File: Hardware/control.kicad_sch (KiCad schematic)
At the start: 4 parts, among them U1 RP2354B, U2 SN74LVC245APW, U3 SN74LVC245APW, U4 SN74LVC8T245

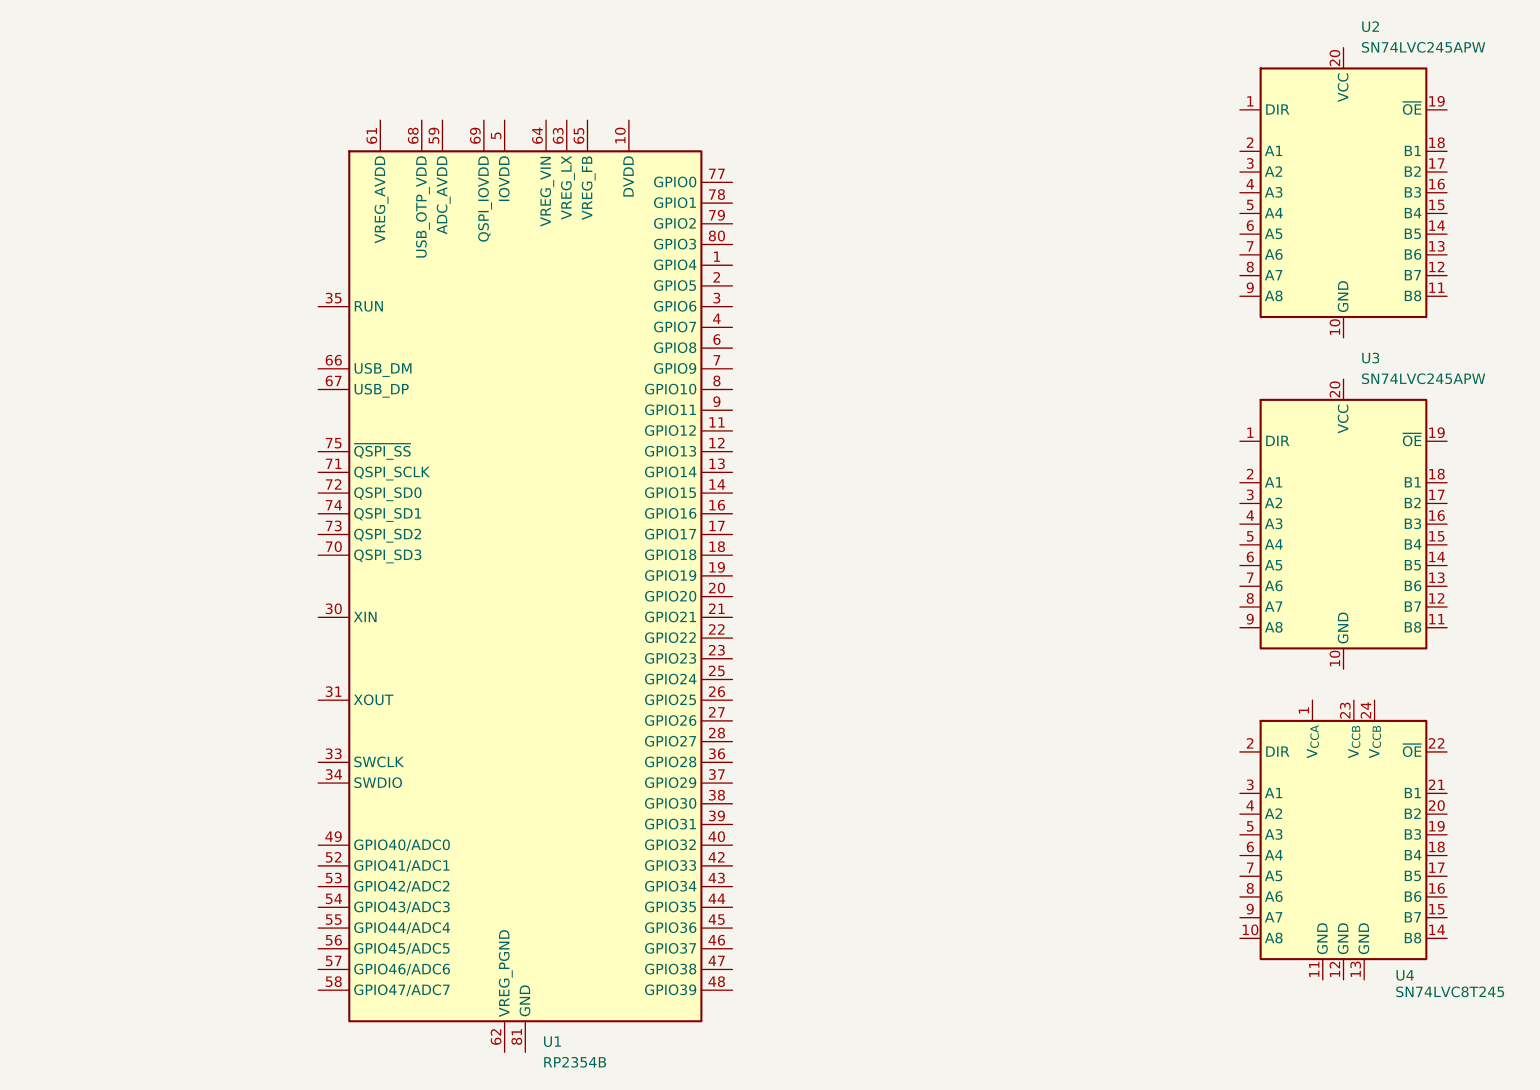
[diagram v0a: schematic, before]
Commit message: fix kicad project hierarchy
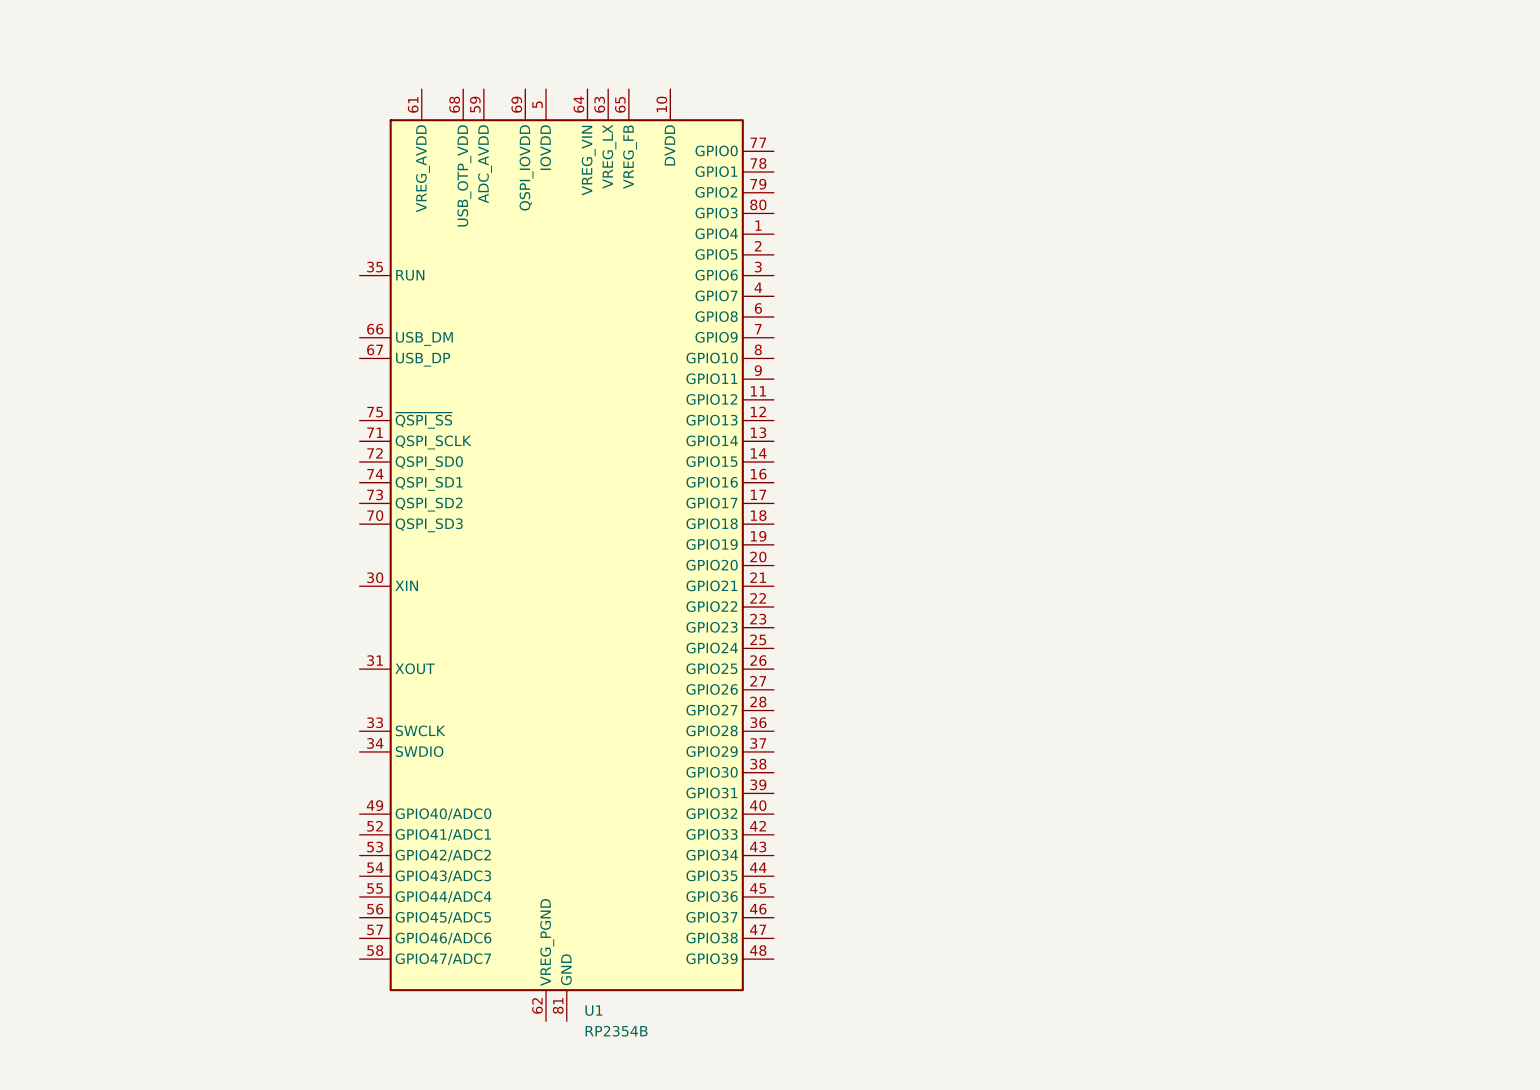
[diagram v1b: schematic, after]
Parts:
- removed U2, U3: SN74LVC245APW, Package_SO:TSSOP-20_4.4x6.5mm_P0.65mm, symbol Logic_LevelTranslator:SN74LVC245APW
- removed U4: SN74LVC8T245, symbol Logic_LevelTranslator:SN74LVC8T245

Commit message: finish digitalker
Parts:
- added X2: ABM8-272-T3, symbol Digichiver:ABM8-272-T3
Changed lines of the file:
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@@
+	)
+	(symbol
+		(lib_id "Digichiver:ABM8-272-T3")
+		(at 165.1 130.81 0)
+		(unit 1)
+		(body_style 1)
+		(exclude_from_sim no)
+		(in_bom yes)
+		(on_board yes)
+		(in_pos_files yes)
+		(dnp no)
+		(fields_autoplaced yes)
+		(property "Reference" "X2"
+			(at 165.1 127 0)
+			(show_name no)
+			(do_not_autoplace no)
+			(effects
+				(font
+					(size 1.27 1.27)
+				)
+			)
+		)
+		(property "Value" "ABM8-272-T3"
+			(at 165.1 129.54 0)
+			(show_name no)
+			(do_not_autoplace no)
+			(effects
+				(font
+					(size 1.27 1.27)
+				)
+			)
+		)
+		(property "Footprint" ""
+			(at 165.1 130.81 0)
+			(hide yes)
+			(show_name no)
+			(do_not_autoplace no)
+			(effects
+				(font
+					(size 1.27 1.27)
+				)
+			)
+		)
+		(property "Datasheet" ""
+			(at 165.1 130.81 0)
+			(hide yes)
+			(show_name no)
+			(do_not_autoplace no)
+			(effects
+				(font
+					(size 1.27 1.27)
+				)
+			)
+		)
+		(property "Description" ""
+			(at 165.1 130.81 0)
+			(hide yes)
+			(show_name no)
+			(do_not_autoplace no)
+			(effects
+				(font
+					(size 1.27 1.27)
+				)
+			)
+		)
+		(pin "1"
+		)
+		(pin "2"
+		)
+		(pin "3"
+		)
+		(pin "4"
+		)
+		(instances
+			(project "digichiver"
+				(path "/51de4045-d2a2-42d9-b145-319acd726bb6/7bd3bb5c-26f1-47ae-a373-5b3a637c22c5"
+					(reference "X2")
+					(unit 1)
+				)
+			)
+		)
 	)
 	(symbol

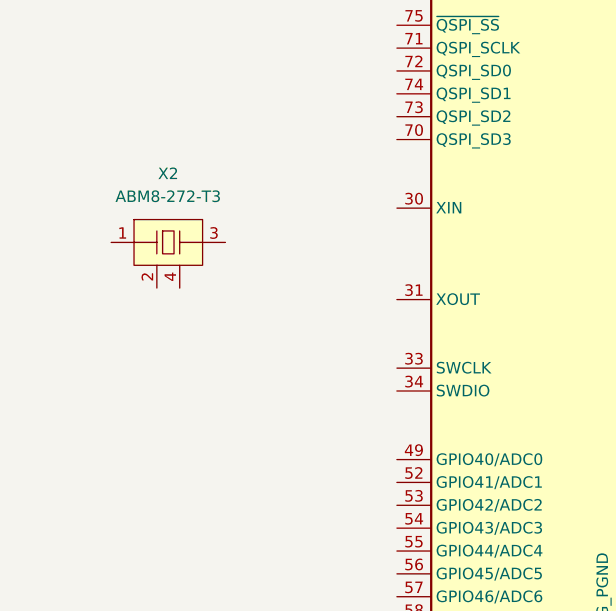
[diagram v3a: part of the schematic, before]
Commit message: add RP2354B crystal
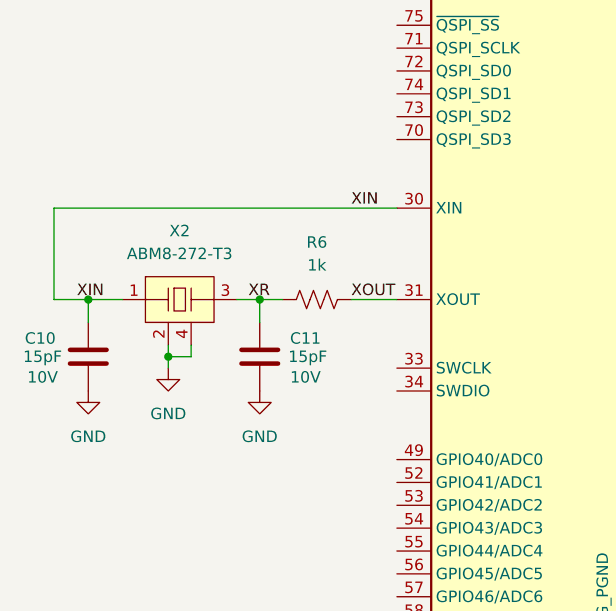
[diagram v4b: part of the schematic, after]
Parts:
- added C10, C11: 15pF, symbol Device:C
- added R6: 1k, symbol Device:R_US
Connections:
- net XIN: now reaches X2.1
- net XIN: now also U1.30 (XIN), C10.1
- net GND: now reaches X2.2
- net GND: now also X2.4, C10.2, C11.2
- net XR: now reaches X2.3
- net XR: now also C11.1, R6.2
- net XOUT: now reaches U1.31 (XOUT)
- net XOUT: now also R6.1
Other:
- moved on the sheet: X2
